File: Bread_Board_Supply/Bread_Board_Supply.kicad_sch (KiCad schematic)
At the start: 27 parts, among them J1 3.3_Connector, J2 5V_Connector, J3 12V_Connector, J4 Barrel_Jack_Switch, SW1 SW_Wuerth_450301014042, U1 TPS562202, U2 LP5907MFX-3.3

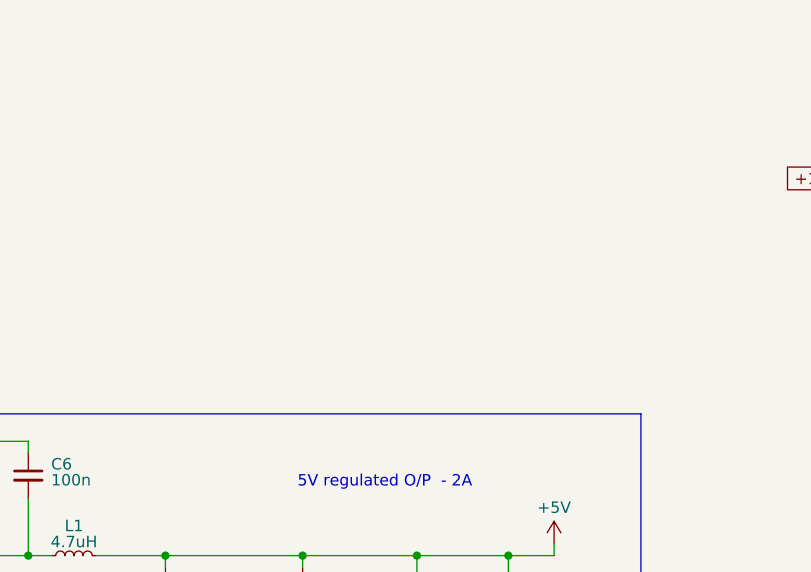
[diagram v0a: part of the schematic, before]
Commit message: USB C added
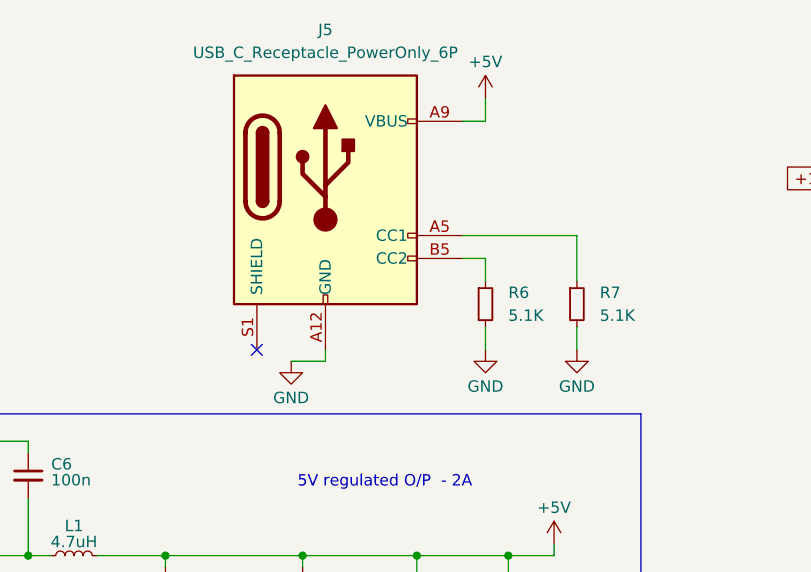
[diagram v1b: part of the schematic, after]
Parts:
- added J5: USB_C_Receptacle_PowerOnly_6P, Connector_USB:USB_C_Receptacle_GCT_USB4125-xx-x_6P_TopMnt_Horizontal, symbol Connector:USB_C_Receptacle_PowerOnly_6P
- added R6, R7: 5.1K, Bread_Board_powers:ERL07_VIS, symbol Device:R_Small
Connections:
- net +5V: now also J5.A9 (VBUS), J5.B9 (VBUS)
- net GND: now also J5.A12 (GND), J5.B12 (GND), R6.2, R7.2
- new net: J5.A5 (CC1), R7.1
- new net: J5.B5 (CC2), R6.1
- no-connect marks 1 -> 2
